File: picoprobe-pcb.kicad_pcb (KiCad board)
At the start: 2 copper layers, 66.1 x 33 mm, 6 parts, among them J1 Conn_01x08, U1 Pico

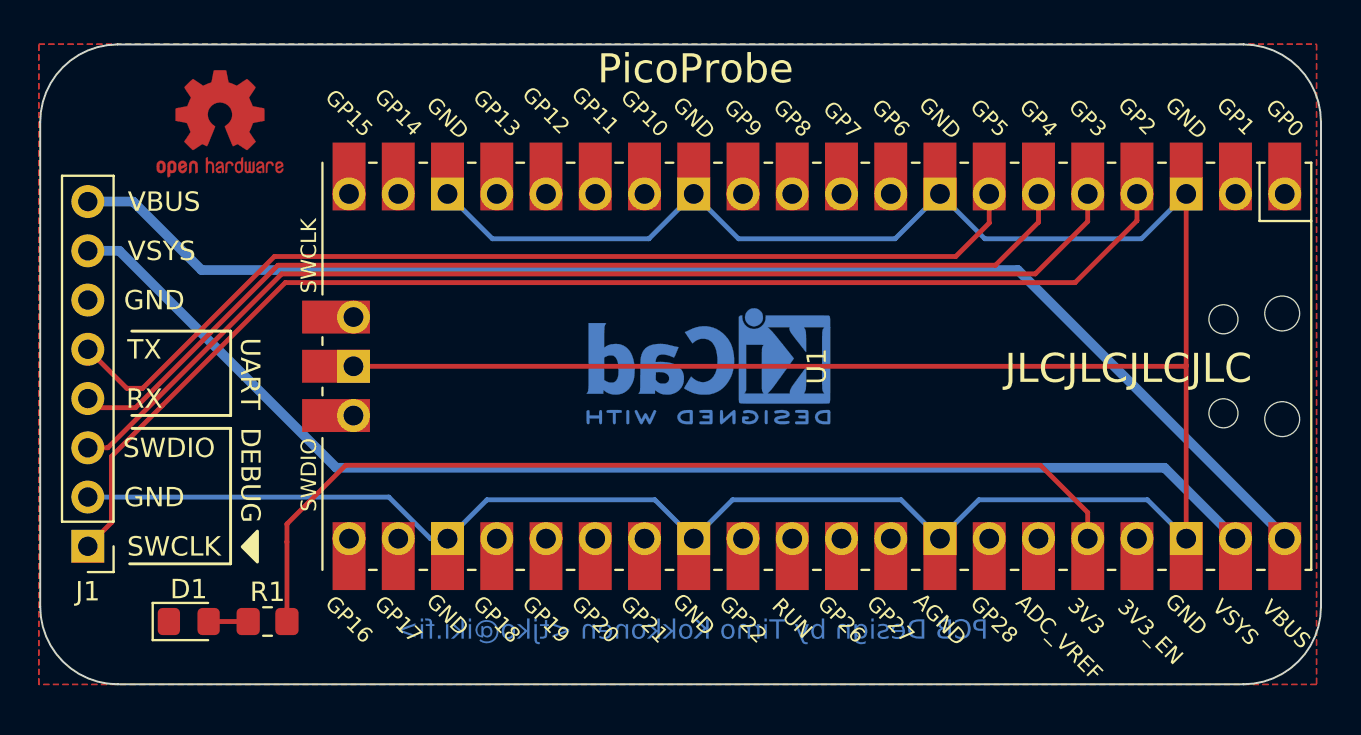
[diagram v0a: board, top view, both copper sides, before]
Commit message: Slightly improved PCB v1.1 and kerbers.
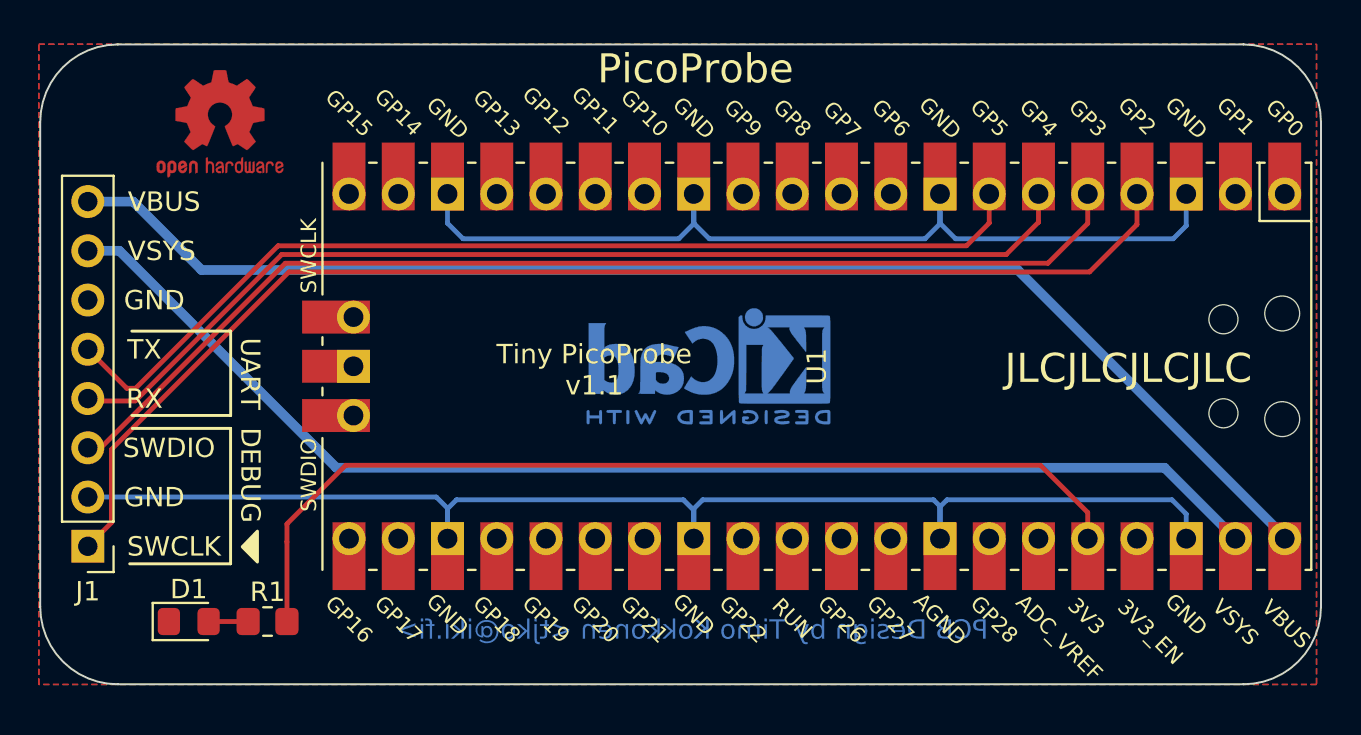
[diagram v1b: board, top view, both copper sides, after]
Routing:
- net GND: track 167.1 -> 118.1 mm
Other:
- board text added: "Tiny PicoProbe v1.1"
